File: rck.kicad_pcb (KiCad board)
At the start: 2 copper layers, 130 x 184 mm, 51 parts, among them J01 Conn_02x22_Row_Letter_Last, J02 Conn_02x22_Row_Letter_Last, J03 Conn_02x22_Row_Letter_Last, J04 Conn_02x22_Row_Letter_Last, J6 Conn_01x06_Pin

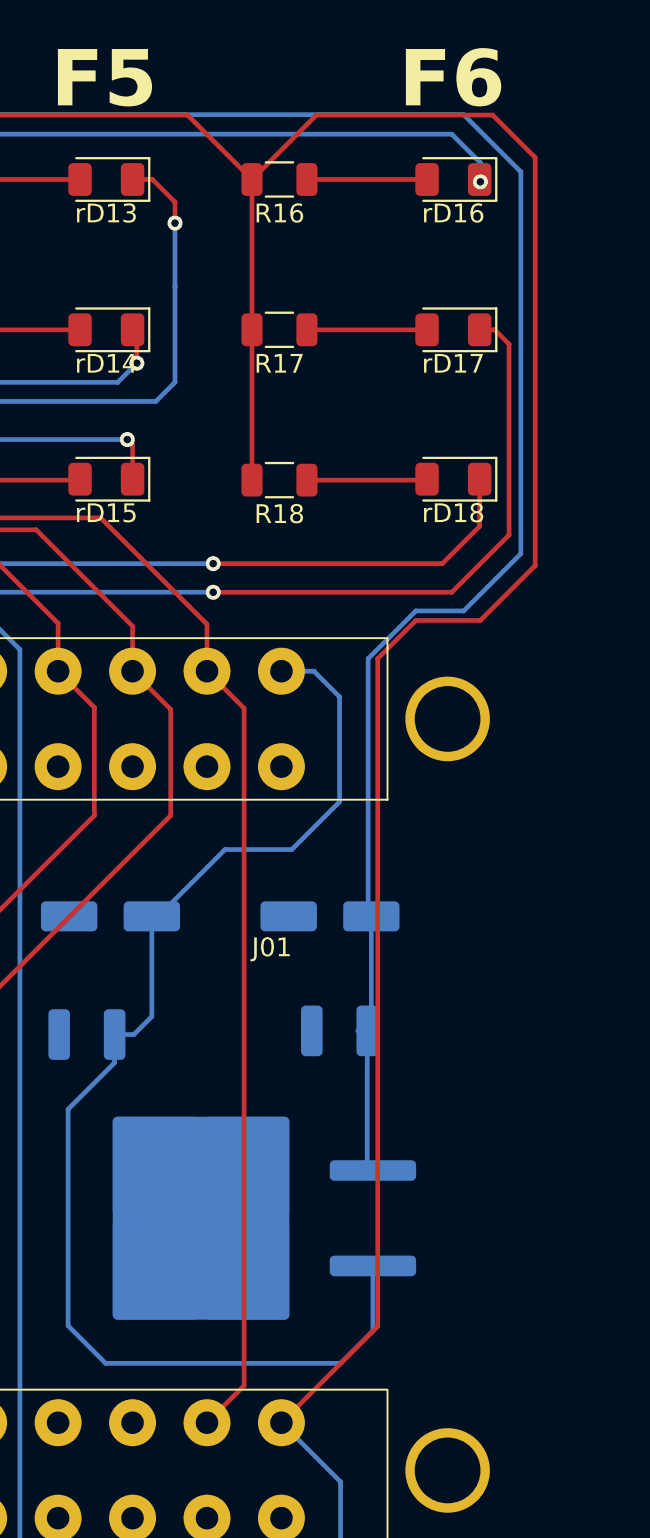
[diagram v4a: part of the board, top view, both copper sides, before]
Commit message: cambio de 7805
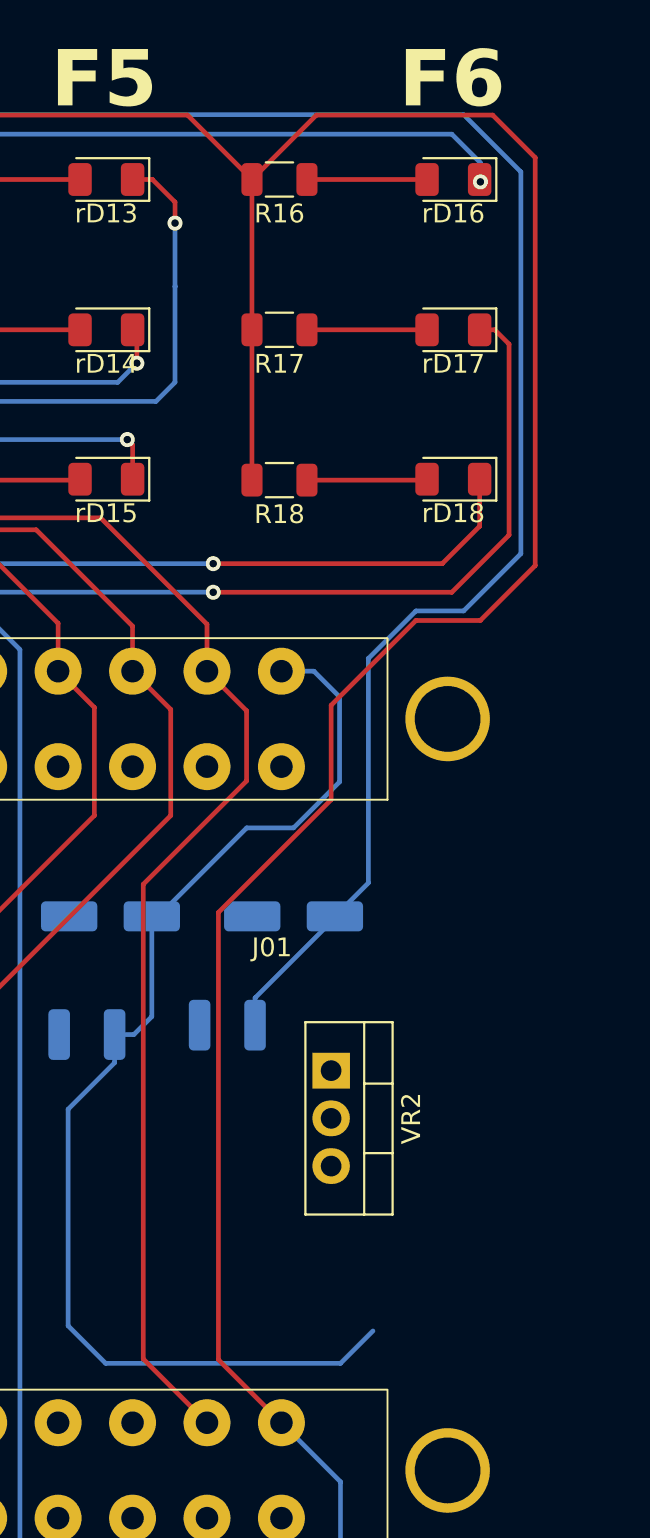
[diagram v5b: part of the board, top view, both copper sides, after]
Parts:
- VR2: footprint Package_TO_SOT_SMD:TO-263-2 -> Package_TO_SOT_THT:TO-220-3_Vertical; moved to F.Cu
- moved VR2 9.55 mm to (145.7, 76.4), turned to -90 degrees
- moved C6 5.98 mm to (140.2, 74.0)
- moved C5 1.94 mm to (143.7, 68.2)
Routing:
- net +12V: track 200.1 -> 192.3 mm
- net +5V: track 67.4 -> 63.3 mm
- net Net-(J01-Pin_2a): track 141.2 -> 144.3 mm
- net VCC: track 416.7 -> 419.5 mm

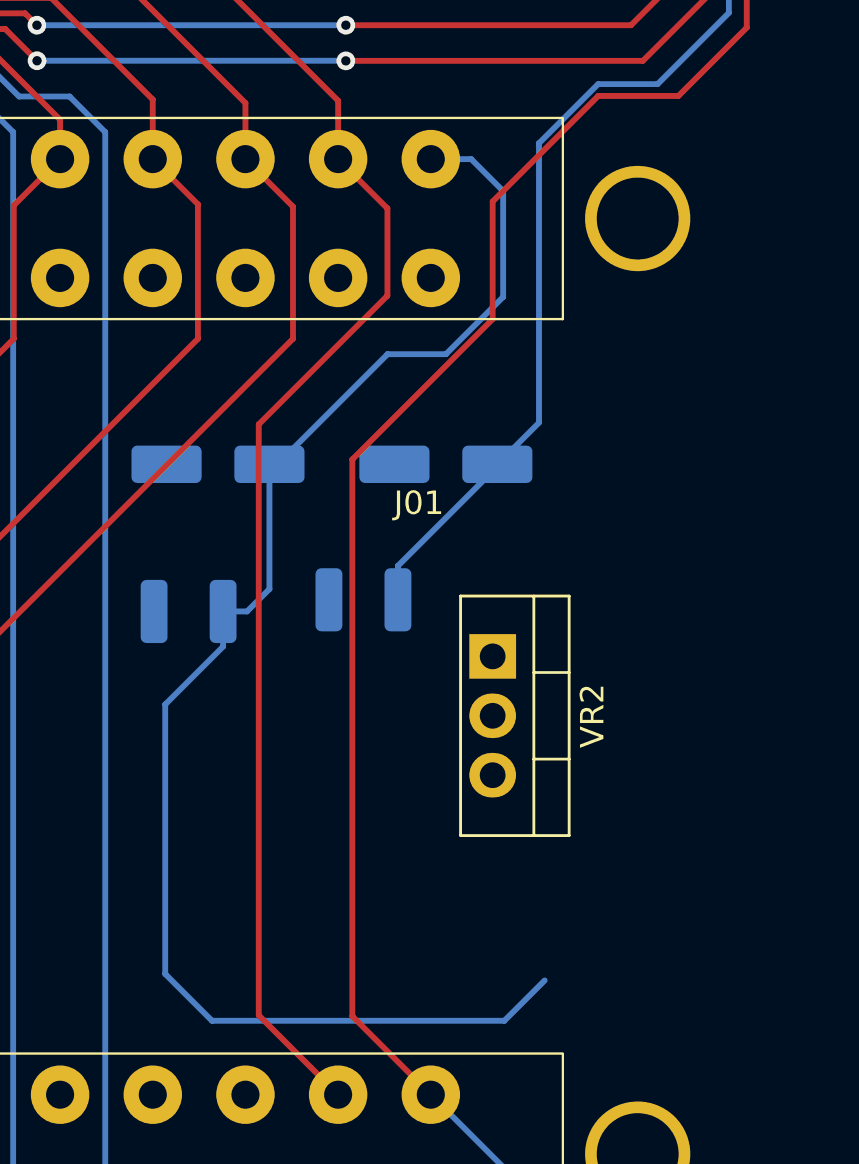
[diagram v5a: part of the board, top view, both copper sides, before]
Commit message: 7805-TO220
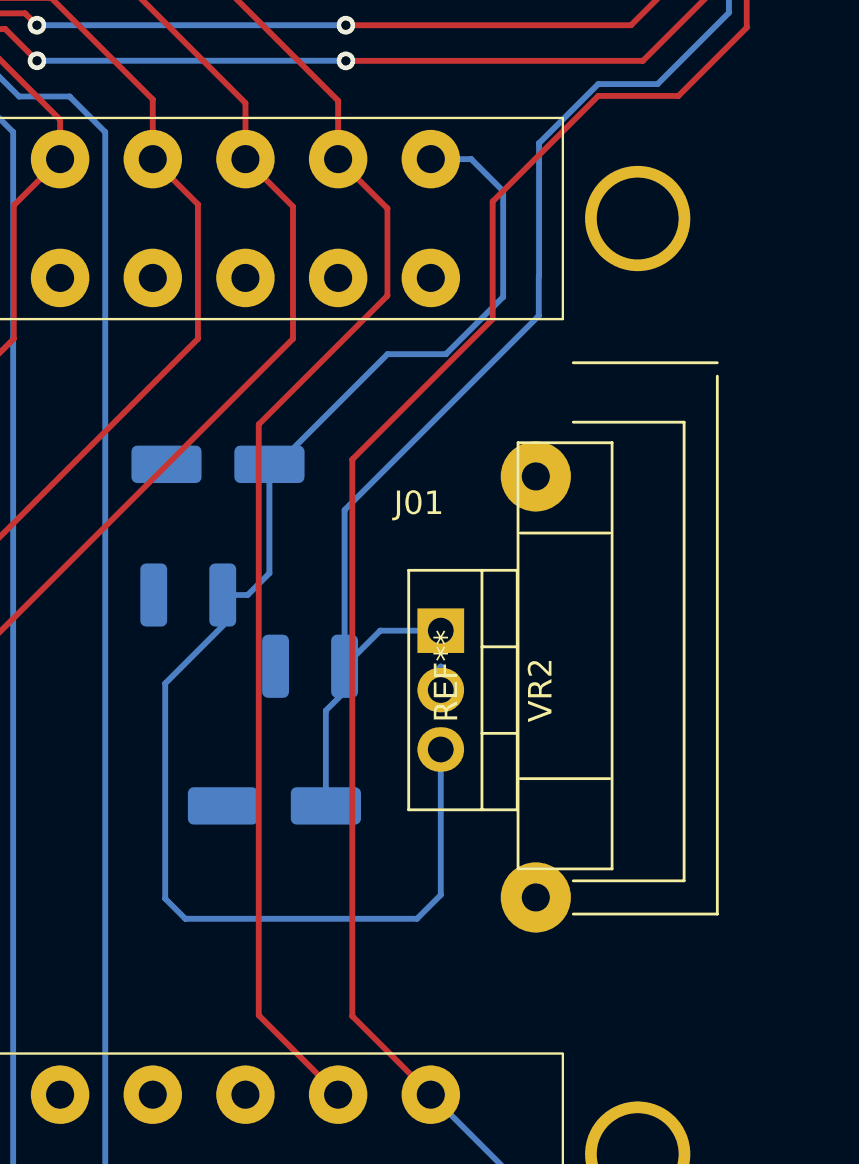
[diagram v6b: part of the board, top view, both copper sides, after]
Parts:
- added REF**: Heatsink_Fischer_FK224xx2201_25x8.3mm, Heatsink:Heatsink_Fischer_FK224xx2201_25x8.3mm, F.Cu at (147.5, 86.7)
- moved C5 16.3 mm to (136.4, 82.8)
- moved C6 3.65 mm to (137.9, 76.8)
- moved VR2 2.48 mm to (143.5, 75.3)
- moved C8 0.70 mm to (132.7, 73.8)
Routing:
- net +12V: track 192.3 -> 207.6 mm
- net +5V: track 63.3 -> 60.4 mm

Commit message: 10F Connected
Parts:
- removed J01, J02, J03, J04: Conn_02x22_Row_Letter_Last, EdgeConectors:Edac_22x2_3.96
- added J1: Conn_02x22_Row_Letter_Last, Library:Edac_22x2_3.96, F.Cu at (143.1, 55.1)
- added J2: Conn_02x22_Row_Letter_Last, Library:Edac_22x2_3.96, F.Cu at (143.1, 95.1)
- added J3: Conn_02x22_Row_Letter_Last, Library:Edac_22x2_3.96, F.Cu at (143.1, 135.1)
- added J4: Conn_02x22_Row_Letter_Last, Library:Edac_22x2_3.96, F.Cu at (143.1, 175.1)
- added J5: Conn_02x22_Row_Letter_Last, Library:Edac_22x2_3.96, F.Cu at (143.1, 215.1)
- added J7: Conn_01x06_Pin, Connector_PinSocket_2.54mm:PinSocket_1x06_P2.54mm_Vertical, F.Cu at (51.1, -6.03)
- J6: value Conn_01x06_Pin -> Conn_02x22_Row_Letter_Last; footprint Connector_PinSocket_2.54mm:PinSocket_1x06_P2.54mm_Vertical -> Library:Edac_22x2_3.96
- moved J6 253.7 mm to (143.1, 255.1), turned to 180 degrees
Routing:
- net /A6-01: track 0.00 -> 308.9 mm, vias 0 -> 1
- net /A6-04: track 0.00 -> 261.8 mm, vias 0 -> 2
- net /A6-03: track 0.00 -> 258.1 mm, vias 0 -> 3
- net /A6-05: track 0.00 -> 241.4 mm, vias 0 -> 4
- net /A6-06: track 0.00 -> 225.8 mm, vias 0 -> 3
- net /A6-02: track 0.00 -> 223.9 mm, vias 0 -> 3
- net /A5-06: track 0.00 -> 184.9 mm, vias 0 -> 1
- net /A5-05: track 0.00 -> 176.3 mm, vias 0 -> 1
- net /A5-03: track 0.00 -> 173.0 mm, vias 0 -> 3
- net /A5-04: track 0.00 -> 172.3 mm, vias 0 -> 1
- net /A5-01: track 0.00 -> 163.6 mm, vias 0 -> 2
- net /A5-02: track 0.00 -> 161.5 mm, vias 0 -> 2
- net VCC: track 419.5 -> 503.9 mm
- net Net-(J1-Pin_5a): track 131.7 -> 126.4 mm
- net Net-(J1-Pin_6a): track 132.2 -> 127.6 mm
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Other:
- board size 130 x 184 mm -> 150 x 267.5 mm

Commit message: update 10F
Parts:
- added R19: R, Resistor_SMD:R_1206_3216Metric, F.Cu at (115.8, 24.6)
- added R20: R, Resistor_SMD:R_1206_3216Metric, F.Cu at (115.8, 32.2)
- added R21: R, Resistor_SMD:R_1206_3216Metric, F.Cu at (115.8, 39.9)
- added R22: R, Resistor_SMD:R_1206_3216Metric, F.Cu at (128.7, 24.6)
- added R23: R, Resistor_SMD:R_1206_3216Metric, F.Cu at (128.7, 32.2)
- added R24: R, Resistor_SMD:R_1206_3216Metric, F.Cu at (128.7, 39.9)
- added R25: R, Resistor_SMD:R_1206_3216Metric, F.Cu at (141.5, 24.6)
- added R26: R, Resistor_SMD:R_1206_3216Metric, F.Cu at (141.5, 32.2)
- added R27: R, Resistor_SMD:R_1206_3216Metric, F.Cu at (141.5, 39.9)
- added R28: R, Resistor_SMD:R_1206_3216Metric, F.Cu at (154.3, 24.6)
- added R29: R, Resistor_SMD:R_1206_3216Metric, F.Cu at (154.3, 32.2)
- added R30: R, Resistor_SMD:R_1206_3216Metric, F.Cu at (154.3, 39.9)
- added rD19: LED, LED_SMD:LED_1206_3216Metric, F.Cu at (122.3, 24.6)
- added rD20: LED, LED_SMD:LED_1206_3216Metric, F.Cu at (122.2, 32.2)
- added rD21: LED, LED_SMD:LED_1206_3216Metric, F.Cu at (122.2, 39.9)
- added rD22: LED, LED_SMD:LED_1206_3216Metric, F.Cu at (135.1, 24.6)
- added rD23: LED, LED_SMD:LED_1206_3216Metric, F.Cu at (135.1, 32.2)
- added rD24: LED, LED_SMD:LED_1206_3216Metric, F.Cu at (135.1, 39.9)
- added rD25: LED, LED_SMD:LED_1206_3216Metric, F.Cu at (147.9, 24.6)
- added rD26: LED, LED_SMD:LED_1206_3216Metric, F.Cu at (147.9, 32.2)
- added rD27: LED, LED_SMD:LED_1206_3216Metric, F.Cu at (147.9, 39.9)
- added rD28: LED, LED_SMD:LED_1206_3216Metric, F.Cu at (160.7, 24.6)
- added rD29: LED, LED_SMD:LED_1206_3216Metric, F.Cu at (160.7, 32.2)
- added rD30: LED, LED_SMD:LED_1206_3216Metric, F.Cu at (160.7, 39.9)
- moved rD18 43.1 mm to (109.4, 39.9)
- moved rD17 43.1 mm to (109.4, 32.2)
- moved rD16 43.0 mm to (109.4, 24.6)
- moved R18 40.3 mm to (103.0, 39.9)
- moved R17 40.2 mm to (103.0, 32.2)
- moved R16 40.2 mm to (103.0, 24.6)
- moved C1 40.1 mm to (53.7, 82.9)
- moved C2 40.1 mm to (53.3, 73.2)
- moved C3 40.1 mm to (74.7, 80.4)
- moved VR1 40.1 mm to (64.4, 76.8)
- moved C4 40.1 mm to (74.7, 72.7)
- moved rD15 37.5 mm to (96.6, 39.9)
- moved rD14 37.5 mm to (96.6, 32.2)
- moved rD13 37.4 mm to (96.6, 24.6)
- moved R15 34.7 mm to (90.2, 39.9)
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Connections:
- net Net-(J1-Pin_10a) renamed /F3-03
- net Net-(J1-Pin_11a) renamed /F4-01
- net Net-(J1-Pin_12a) renamed /F4-02
- net Net-(J1-Pin_13a) renamed /F4-03
- net Net-(J1-Pin_14a) renamed /F5-01
- net Net-(J1-Pin_15a) renamed /F5-02
- net Net-(J1-Pin_16a) renamed /F5-03
- net Net-(J1-Pin_17a) renamed /F6-01
- net Net-(J1-Pin_18a) renamed /F6-02
- net Net-(J1-Pin_19a) renamed /F6-03
- net Net-(J1-Pin_2a) renamed /F1-01
- net Net-(J1-Pin_3a) renamed /F1-02
- net Net-(J1-Pin_4a) renamed /F1-03
- net Net-(J1-Pin_5a) renamed /F2-01
- net Net-(J1-Pin_6a) renamed /F2-02
- net Net-(J1-Pin_7a) renamed /F2-03
- net Net-(J1-Pin_8a) renamed /F3-01
- net Net-(J1-Pin_9a) renamed /F3-02
- J1 pad 10b: /A6-04 -> /F10-03
- J1 pad 11b: /A6-05 -> unconnected-(J1-Pin_11b-Pad11b)
- J1 pad 12b: /A6-06 -> unconnected-(J1-Pin_12b-Pad12b)
- J1 pad 1a: +5V -> VCC
- J1 pad 1b: /A5-01 -> /F7-03
- J1 pad 20a: unconnected-(J1-Pin_20a-Pad20a) -> /F7-01
- J1 pad 21a: unconnected-(J1-Pin_21a-Pad21a) -> /F7-02
- J1 pad 2b: /A5-02 -> /F8-01
- J1 pad 3b: /A5-03 -> /F8-02
- J1 pad 4b: /A5-04 -> /F8-03
- J1 pad 5b: /A5-05 -> /F9-01
- J1 pad 6b: /A5-06 -> /F9-02
- J1 pad 7b: /A6-01 -> /F9-03
- J1 pad 8b: /A6-02 -> /F10-01
- J1 pad 9b: /A6-03 -> /F10-02
- J5 pad 10a: /A5-03 -> /F7-03
- J5 pad 14a: /A5-04 -> /F8-01
- J5 pad 18a: /A5-05 -> /F8-02
- J5 pad 22a: /A5-06 -> /F8-03
- J5 pad 2a: /A5-01 -> /F7-01
- J5 pad 6a: /A5-02 -> /F7-02
- J6 pad 10a: /A6-03 -> /F9-03
- J6 pad 14a: /A6-04 -> /F10-01
- J6 pad 18a: /A6-05 -> /F10-02
- J6 pad 22a: /A6-06 -> /F10-03
- J6 pad 2a: /A6-01 -> /F9-01
- J6 pad 6a: /A6-02 -> /F9-02
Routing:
- net VCC: track 503.9 -> 152.9 mm, vias 1 -> 0
- net /A6-01: track 308.9 -> 0.00 mm, vias 1 -> 0
- net /F5-01: track 273.2 -> 0.00 mm, vias 3 -> 0
- net /A6-04: track 261.8 -> 0.00 mm, vias 2 -> 0
- net /A6-03: track 258.1 -> 0.00 mm, vias 3 -> 0
- net /F6-01: track 254.3 -> 0.00 mm, vias 1 -> 0
- net /F5-02: track 246.1 -> 0.00 mm, vias 3 -> 0
- net /A6-05: track 241.4 -> 0.00 mm, vias 4 -> 0
- net /F6-02: track 234.9 -> 0.00 mm, vias 2 -> 0
- net /F5-03: track 231.1 -> 0.00 mm, vias 1 -> 0
- net /A6-06: track 225.8 -> 0.00 mm, vias 3 -> 0
- net /A6-02: track 223.9 -> 0.00 mm, vias 3 -> 0
- net /F6-03: track 219.6 -> 0.00 mm, vias 2 -> 0
- net /F4-01: track 197.8 -> 0.00 mm, vias 3 -> 0
- net /F4-02: track 191.0 -> 0.00 mm, vias 3 -> 0
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- removed copper zone on B.Cu, net GND
- removed copper zone on F.Cu, net GND
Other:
- board size 150 x 267.5 mm -> 150 x 285 mm
- board text added: "F10"
- board text added: "F7"
- board text added: "F8"
- board text added: "F9"
